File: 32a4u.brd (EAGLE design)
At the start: 29.2 x 49.5 mm, 11 parts

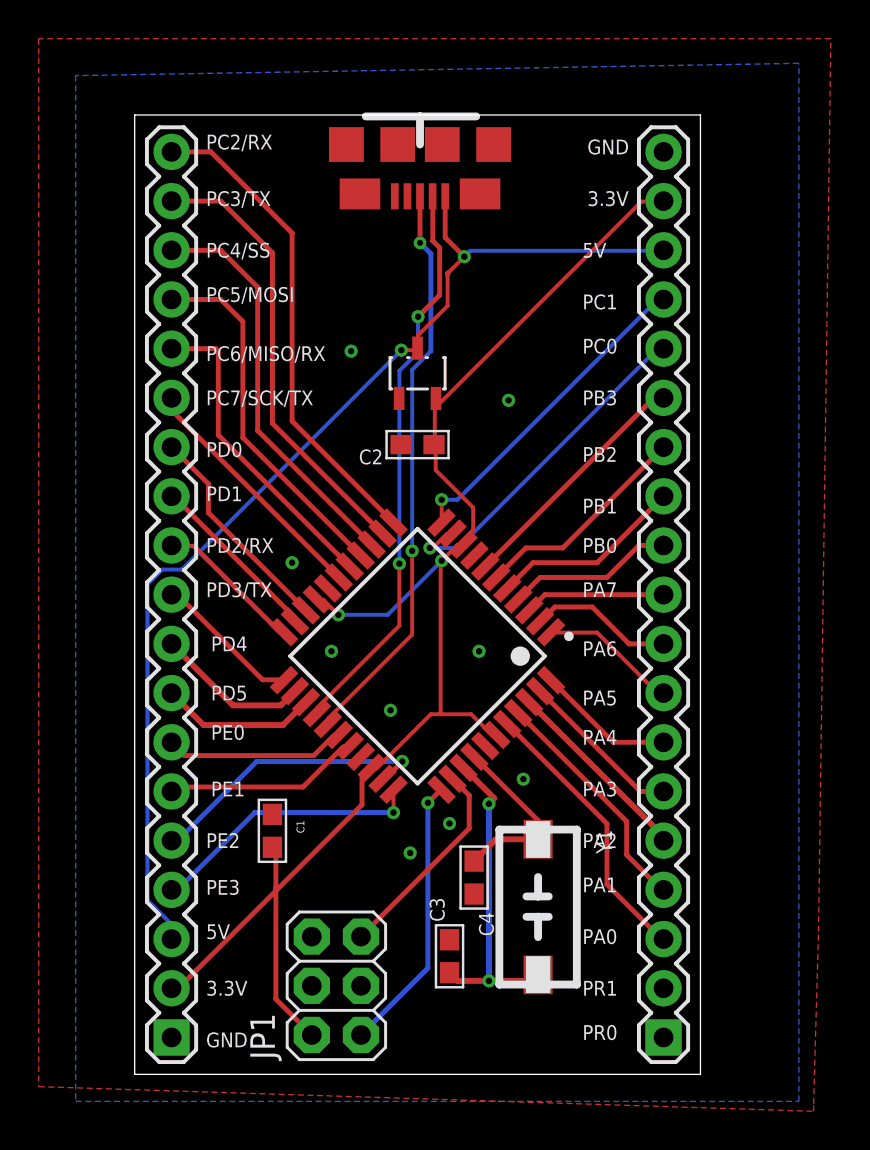
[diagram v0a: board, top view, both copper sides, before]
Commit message: tweak traces, standardize labeling
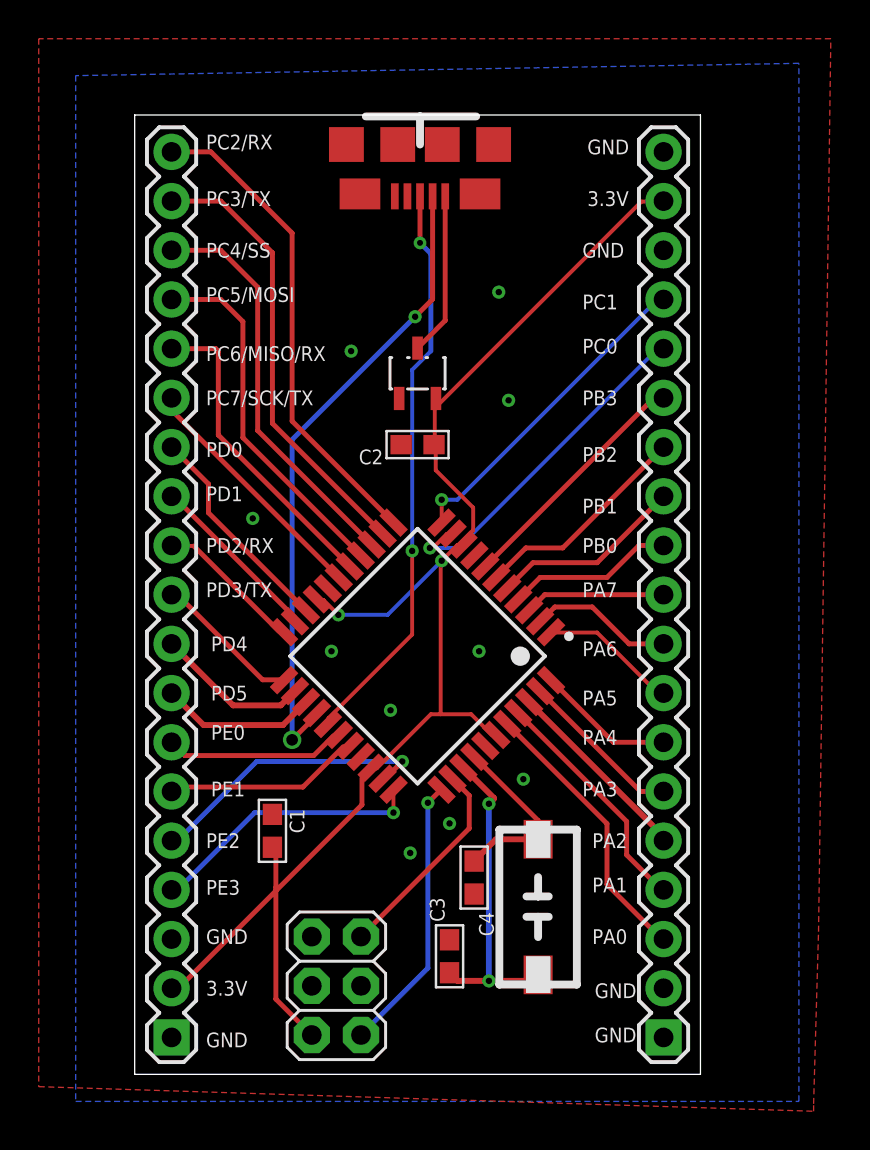
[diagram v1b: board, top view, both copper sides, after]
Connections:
- net GND: now also U$3.1, U$3.17, U$3.2, U$4.3
- net VUSB: no longer U$3.17, U$4.3
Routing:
- net VUSB: track 57.5 -> 8.43 mm, vias 2 -> 0
- net USB-: track 29.5 -> 33.0 mm
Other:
- board text removed: "5V"
- board text removed: "PR0"
- board text removed: "PR1"

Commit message: passes fusion DRC
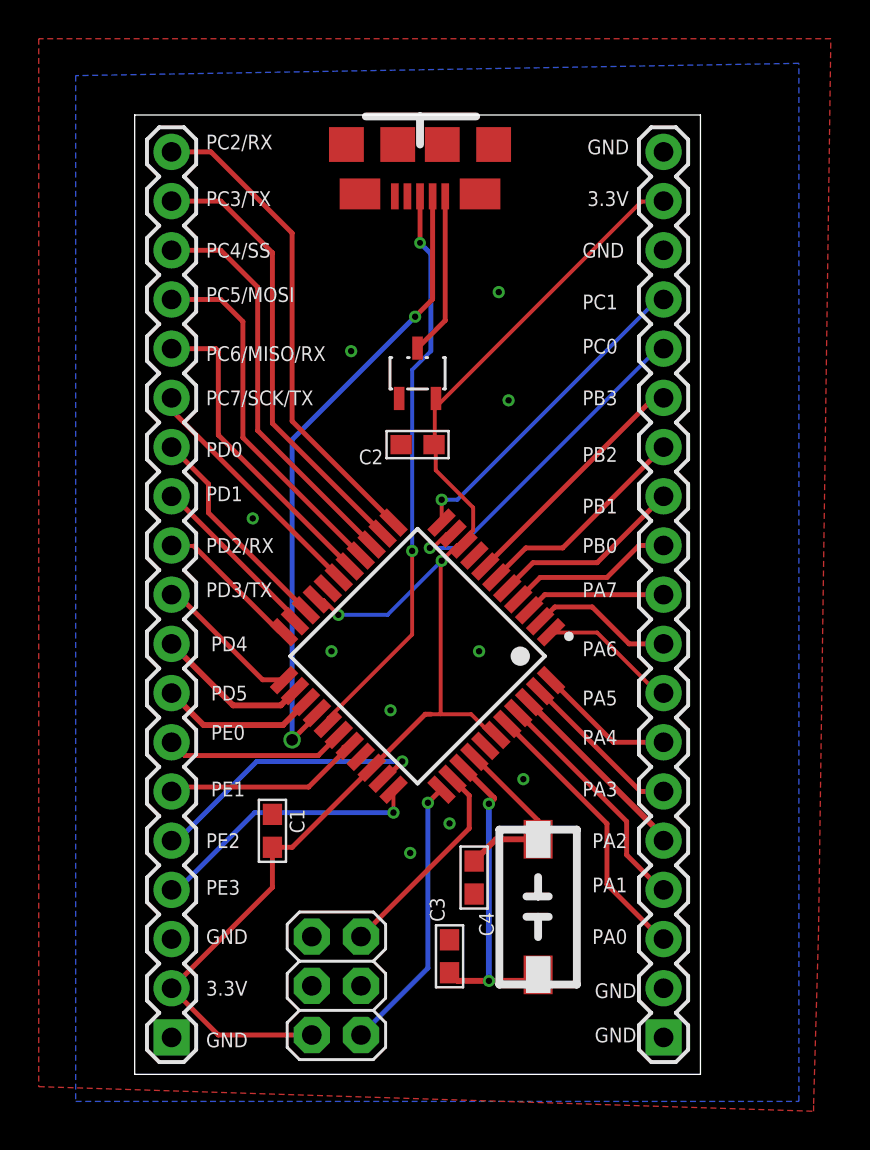
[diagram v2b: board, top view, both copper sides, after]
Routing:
- net VCC: track 77.4 -> 75.4 mm
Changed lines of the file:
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@@
 </class>
 </classes>
-<designrules name="LaenPCBOrder">
+<designrules name="Fusion_eagle_rule_v1.1">
 <description language="de">&lt;b&gt;EAGLE Design Rules&lt;/b&gt;
 &lt;p&gt;
@@
 Einstellungen hier und speichern die Design Rules unter
 einem neuen Namen ab.</description>
-<description language="en">&lt;b&gt;Laen's PCB Order Design Rules&lt;/b&gt;
+<description language="en">&lt;b&gt;EAGLE Design Rules&lt;/b&gt;
 &lt;p&gt;
-Please make sure your boards conform to these design rules.</description>
+The default Design Rules have been set to cover
+a wide range of applications. Your particular design
+may have different requirements, so please make the
+necessary adjustments and save your customized
+design rules under a new name.</description>
+<description language="zh">&lt;b&gt;Seeed Studio EAGLE Design Rules&lt;/b&gt;
+</description>
 <param name="layerSetup" value="(1*16)"/>
-<param name="mtCopper" value="0.0356mm 0.0356mm 0.0356mm 0.0356mm 0.0356mm 0.0356mm 0.0356mm 0.0356mm 0.0356mm 0.0356mm 0.0356mm 0.0356mm 0.0356mm 0.0356mm 0.0356mm 0.0356mm"/>
-<param name="mtIsolate" value="1.5011mm 0.1499mm 0.2007mm 0.1499mm 0.2007mm 0.1499mm 0.2007mm 0.1499mm 0.2007mm 0.1499mm 0.2007mm 0.1499mm 0.2007mm 0.1499mm 0.2007mm"/>
+<param name="mtCopper" value="0.035mm 0.035mm 0.035mm 0.035mm 0.035mm 0.035mm 0.035mm 0.035mm 0.035mm 0.035mm 0.035mm 0.035mm 0.035mm 0.035mm 0.035mm 0.035mm"/>
+<param name="mtIsolate" value="1.5mm 0.15mm 0.2mm 0.15mm 0.2mm 0.15mm 0.2mm 0.15mm 0.2mm 0.15mm 0.2mm 0.15mm 0.2mm 0.15mm 0.2mm"/>
 <param name="mdWireWire" value="6mil"/>
 <param name="mdWirePad" value="6mil"/>
@@
 <param name="mdPadVia" value="6mil"/>
 <param name="mdViaVia" value="6mil"/>
-<param name="mdSmdPad" value="6mil"/>
-<param name="mdSmdVia" value="6mil"/>
-<param name="mdSmdSmd" value="6mil"/>
+<param name="mdSmdPad" value="0mil"/>
+<param name="mdSmdVia" value="0mil"/>
+<param name="mdSmdSmd" value="0mil"/>
 <param name="mdViaViaSameLayer" value="8mil"/>
 <param name="mnLayersViaInSmd" value="2"/>
-<param name="mdCopperDimension" value="15mil"/>
-<param name="mdDrill" value="6mil"/>
+<param name="mdCopperDimension" value="10mil"/>
+<param name="mdDrill" value="10mil"/>
 <param name="mdSmdStop" value="0mil"/>
 <param name="msWidth" value="6mil"/>
-<param name="msDrill" value="13mil"/>
-<param name="msMicroVia" value="13mil"/>
+<param name="msDrill" value="12mil"/>
+<param name="msMicroVia" value="12mil"/>
 <param name="msBlindViaRatio" value="0.5"/>
 <param name="rvPadTop" value="0.25"/>
@@
 <param name="rvMicroViaOuter" value="0.25"/>
 <param name="rvMicroViaInner" value="0.25"/>
-<param name="rlMinPadTop" value="7mil"/>
+<param name="rlMinPadTop" value="10mil"/>
 <param name="rlMaxPadTop" value="20mil"/>
-<param name="rlMinPadInner" value="7mil"/>
+<param name="rlMinPadInner" value="10mil"/>
 <param name="rlMaxPadInner" value="20mil"/>
-<param name="rlMinPadBottom" value="7mil"/>
+<param name="rlMinPadBottom" value="10mil"/>
 <param name="rlMaxPadBottom" value="20mil"/>
-<param name="rlMinViaOuter" value="7mil"/>
+<param name="rlMinViaOuter" value="6mil"/>
 <param name="rlMaxViaOuter" value="20mil"/>
-<param name="rlMinViaInner" value="7mil"/>
+<param name="rlMinViaInner" value="6mil"/>
 <param name="rlMaxViaInner" value="20mil"/>
 <param name="rlMinMicroViaOuter" value="4mil"/>
@@
 <param name="psTop" value="-1"/>
 <param name="psBottom" value="-1"/>
-<param name="psFirst" value="-1"/>
+<param name="psFirst" value="0"/>
 <param name="psElongationLong" value="100"/>
 <param name="psElongationOffset" value="100"/>
 <param name="mvStopFrame" value="1"/>
 <param name="mvCreamFrame" value="0"/>
-<param name="mlMinStopFrame" value="4mil"/>
-<param name="mlMaxStopFrame" value="4mil"/>
+<param name="mlMinStopFrame" value="2mil"/>
+<param name="mlMaxStopFrame" value="2mil"/>
 <param name="mlMinCreamFrame" value="0mil"/>
 <param name="mlMaxCreamFrame" value="0mil"/>
-<param name="mlViaStopLimit" value="0mil"/>
+<param name="mlViaStopLimit" value="100mil"/>
 <param name="srRoundness" value="0"/>
 <param name="srMinRoundness" value="0mil"/>
@@
 <param name="checkAngle" value="0"/>
 <param name="checkFont" value="1"/>
-<param name="checkRestrict" value="1"/>
+<param name="checkRestrict" value="0"/>
 <param name="useDiameter" value="13"/>
 <param name="maxErrors" value="50"/>
@@
 <contactref element="U$3" pad="18"/>
 <contactref element="U$4" pad="2"/>
-<wire x1="14.2748" y1="15.1892" x2="14.2748" y2="16.5608" width="0.254" layer="1"/>
-<wire x1="14.2748" y1="16.5608" x2="14.7828" y2="17.0688" width="0.2032" layer="1"/>
-<wire x1="14.7828" y1="17.0688" x2="14.776190625" y2="17.097078125" width="0.2032" layer="1"/>
 <wire x1="20.9804" y1="18.796" x2="21.1836" y2="18.796" width="0.2032" layer="1"/>
 <wire x1="19.9136" y1="19.8628" x2="20.9804" y2="18.796" width="0.2032" layer="1"/>
 <wire x1="17.8308" y1="19.8628" x2="18.3388" y2="19.8628" width="0.2032" layer="1"/>
 <wire x1="18.3388" y1="19.8628" x2="19.9136" y2="19.8628" width="0.2032" layer="1"/>
-<wire x1="15.0368" y1="17.0688" x2="17.8308" y2="19.8628" width="0.2032" layer="1"/>
-<wire x1="14.8844" y1="17.0688" x2="15.0368" y2="17.0688" width="0.2032" layer="1"/>
 <wire x1="21.1836" y1="18.796" x2="21.2108625" y2="18.794134375" width="0.2032" layer="1"/>
-<wire x1="14.776190625" y1="17.097078125" x2="14.8844" y2="17.0688" width="0.2032" layer="1"/>
-<wire x1="4.4704" y1="5.7404" x2="4.826" y2="5.7404" width="0.2032" layer="1"/>
-<wire x1="4.445" y1="5.715" x2="4.4704" y2="5.7404" width="0.2032" layer="1"/>
-<wire x1="4.826" y1="5.7404" x2="9.8298" y2="10.7442" width="0.254" layer="1"/>
-<wire x1="9.8298" y1="10.7442" x2="14.2748" y2="15.1892" width="0.254" layer="1"/>
 <wire x1="18.034" y1="33.782" x2="18.034" y2="36.068" width="0.2032" layer="1"/>
 <wire x1="18.034" y1="36.068" x2="18.0848" y2="36.1188" width="0.2032" layer="1"/>
@@
 <via x="18.3896" y="27.7876" extent="1-16" drill="0.3302"/>
 <contactref element="JP1" pad="2"/>
-<wire x1="9.652" y1="12.993" x2="9.8298" y2="12.8152" width="0.254" layer="1"/>
-<wire x1="9.8298" y1="12.8152" x2="9.8298" y2="10.922" width="0.254" layer="1"/>
-<wire x1="9.8298" y1="10.922" x2="9.8298" y2="10.7442" width="0.254" layer="1"/>
-<wire x1="11.684" y1="3.302" x2="9.8298" y2="5.1562" width="0.254" layer="1"/>
-<wire x1="9.8298" y1="5.1562" x2="9.8298" y2="10.7442" width="0.254" layer="1"/>
+<wire x1="17.8308" y1="19.8628" x2="17.5419125" y2="19.8628" width="0.254" layer="1"/>
+<wire x1="17.5419125" y1="19.8628" x2="14.776190625" y2="17.097078125" width="0.254" layer="1"/>
+<wire x1="14.776190625" y1="17.097078125" x2="10.6721125" y2="12.993" width="0.254" layer="1"/>
+<wire x1="10.6721125" y1="12.993" x2="9.652" y2="12.993" width="0.254" layer="1"/>
+<wire x1="4.445" y1="5.715" x2="9.652" y2="10.922" width="0.254" layer="1"/>
+<wire x1="9.652" y1="10.922" x2="9.652" y2="12.993" width="0.254" layer="1"/>
+<wire x1="11.684" y1="3.302" x2="6.858" y2="3.302" width="0.254" layer="1"/>
+<wire x1="6.858" y1="3.302" x2="4.445" y2="5.715" width="0.254" layer="1"/>
 </signal>
 <signal name="VUSB">
@@
 <contactref element="ATXMEGA32A4U" pad="28"/>
 <contactref element="U$4" pad="7"/>
-<wire x1="12.8016" y1="18.7452" x2="13.0556" y2="18.7452" width="0.2032" layer="1"/>
-<wire x1="11.7856" y1="17.7292" x2="12.8016" y2="18.7452" width="0.254" layer="1"/>
-<wire x1="5.1308" y1="17.7292" x2="11.7856" y2="17.7292" width="0.254" layer="1"/>
+<wire x1="5.1308" y1="17.7292" x2="12.0142" y2="17.7292" width="0.254" layer="1"/>
 <wire x1="13.0556" y1="18.7452" x2="13.079134375" y2="18.794134375" width="0.2032" layer="1"/>
 <wire x1="4.445" y1="18.415" x2="5.1308" y2="17.7292" width="0.254" layer="1"/>
+<wire x1="12.0142" y1="17.7292" x2="13.079134375" y2="18.794134375" width="0.254" layer="1"/>
 </signal>
 <signal name="PE1">
@@
 <contactref element="U$4" pad="6"/>
 <wire x1="13.3096" y1="18.1864" x2="13.6144" y2="18.1864" width="0.2032" layer="1"/>
-<wire x1="11.2268" y1="16.1036" x2="13.3096" y2="18.1864" width="0.254" layer="1"/>
-<wire x1="4.6736" y1="16.1036" x2="11.2268" y2="16.1036" width="0.254" layer="1"/>
+<wire x1="4.6736" y1="16.1036" x2="11.51996875" y2="16.1036" width="0.254" layer="1"/>
 <wire x1="13.6144" y1="18.1864" x2="13.64481875" y2="18.22845" width="0.2032" layer="1"/>
 <wire x1="4.445" y1="15.875" x2="4.6736" y2="16.1036" width="0.254" layer="1"/>
+<wire x1="11.51996875" y1="16.1036" x2="13.64481875" y2="18.22845" width="0.254" layer="1"/>
 </signal>
 <signal name="PE2">

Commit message: Clean up:   * Route USB as a differential pair   * Route crystal more efficiently   * Power plane for VCC distribution
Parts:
- moved C3 8.30 mm to (22.1, 15.0), turned to 0 degrees
- moved C4 4.10 mm to (23.9, 13.0), turned to 0 degrees
- moved Y1 2.84 mm to (20.6, 9.40), turned to 180 degrees
- moved C2 2.03 mm to (17.1, 35.8)
- moved JP1 1.52 mm to (13.0, 4.32), turned to 180 degrees
- moved U$2 1.52 mm to (17.1, 39.0)
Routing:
- net VCC: track 75.4 -> 81.8 mm, vias 2 -> 0
- net GND: track 0.00 -> 5.69 mm, vias 10 -> 17
- net PR0: track 16.6 -> 11.6 mm, vias 2 -> 0
- net PDI-CLK: track 10.8 -> 15.2 mm
- net USB-: track 33.0 -> 29.4 mm
- net PC0: track 17.8 -> 15.1 mm, vias 1 -> 0
- net PDI-DATA: track 14.4 -> 12.5 mm
- net VUSB: track 8.43 -> 7.28 mm
- net PR1: track 9.39 -> 10.3 mm
- net PC1: track 16.9 -> 16.3 mm, vias 1 -> 0
- added copper zone on layer 1, net VCC
